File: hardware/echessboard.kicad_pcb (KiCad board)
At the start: 2 copper layers, 205 x 170 mm, 165 parts, among them J1 Conn_01x04_Pin, J3 USB_C_Receptacle_USB2.0_16P, J4 Conn_01x05_Pin, SW1 SW_Push, SW2 SW_Push, SW3 SW_Push, SW4 SW_Push, SW5 SW_Push, U1 STM32F030C6Tx, U3 USBLC6-2P6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

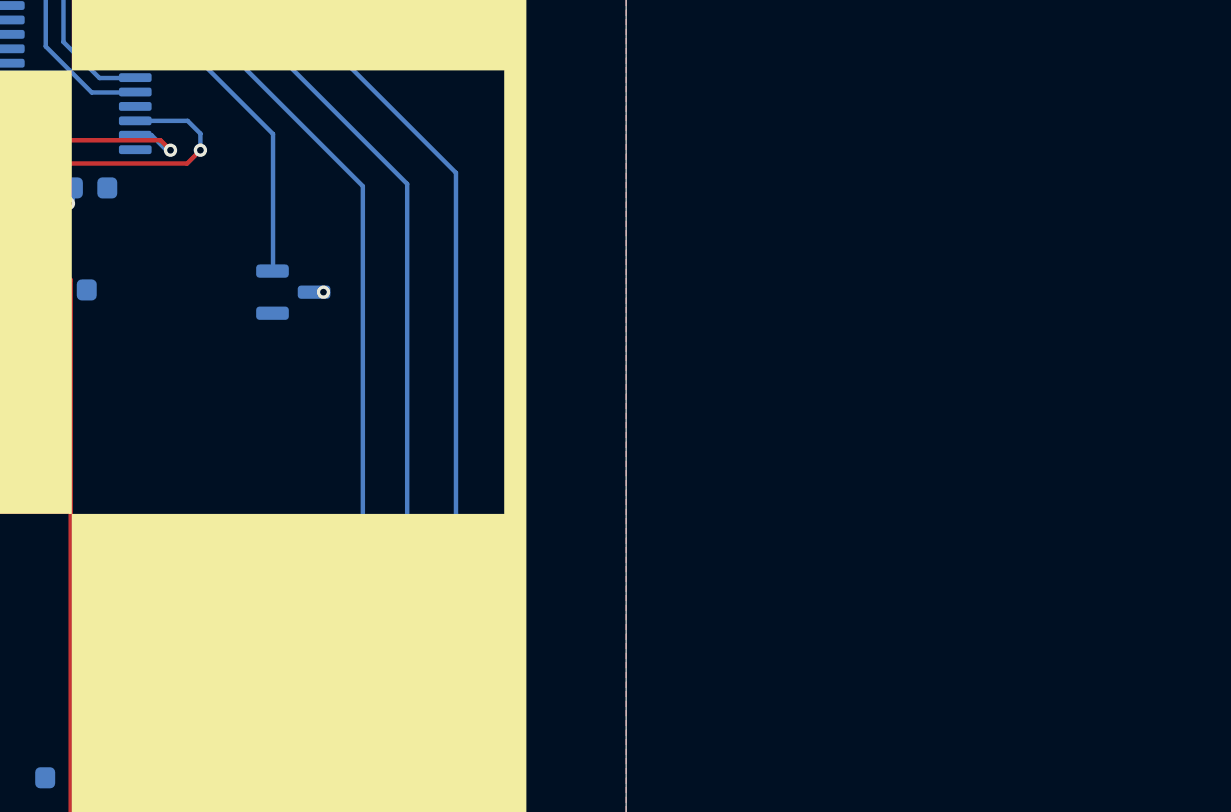
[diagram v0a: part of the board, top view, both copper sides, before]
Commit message: fix i2c pins
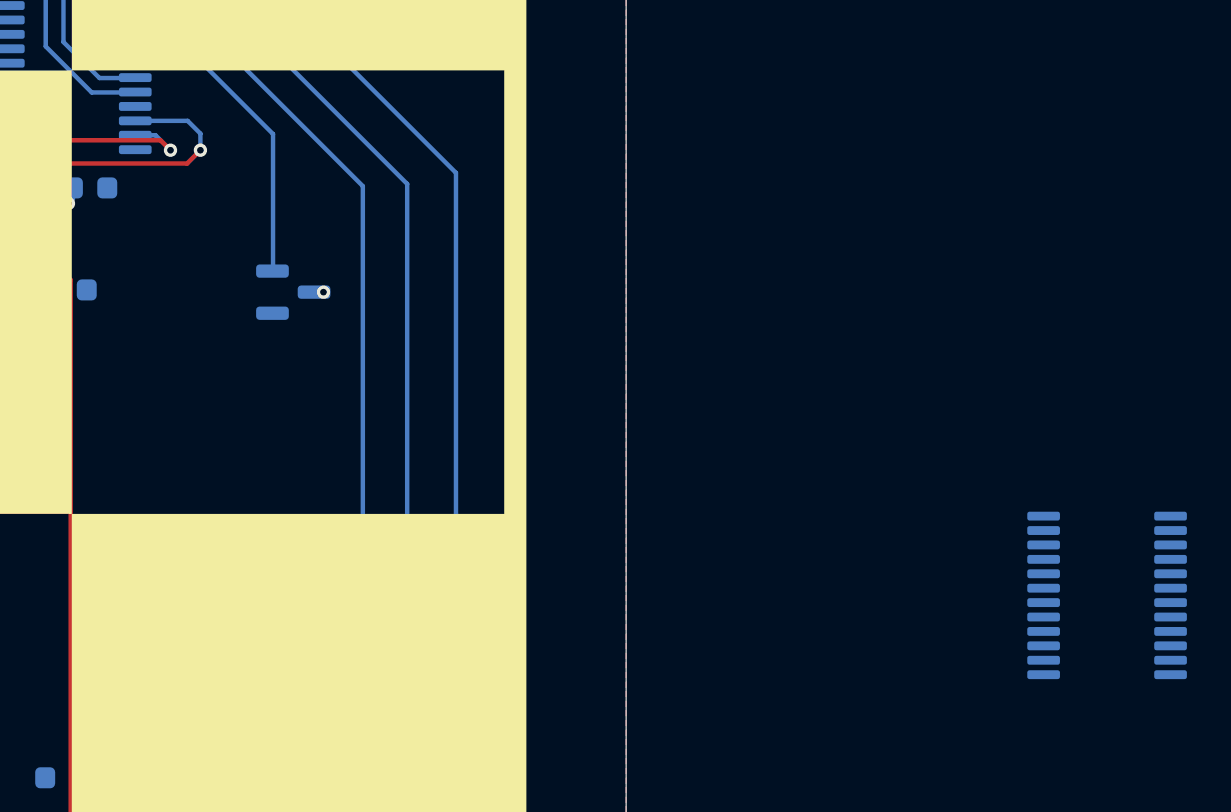
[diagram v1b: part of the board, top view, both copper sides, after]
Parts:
- added IO5: TCA9535PWR, Package_SO:TSSOP-24_4.4x7.8mm_P0.65mm, B.Cu at (301.7, 163.7)

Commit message: read working
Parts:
- removed IO5: TCA9535PWR, Package_SO:TSSOP-24_4.4x7.8mm_P0.65mm
